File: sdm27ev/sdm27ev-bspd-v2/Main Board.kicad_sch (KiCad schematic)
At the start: 41 parts, among them IC301 L7805ACD2T-TR, IC302 74AHC1G08, IC303 SN74LVC1G17DBVRG4, IC304 SN74HC32PWR, U301 TLV9022QDRQ1

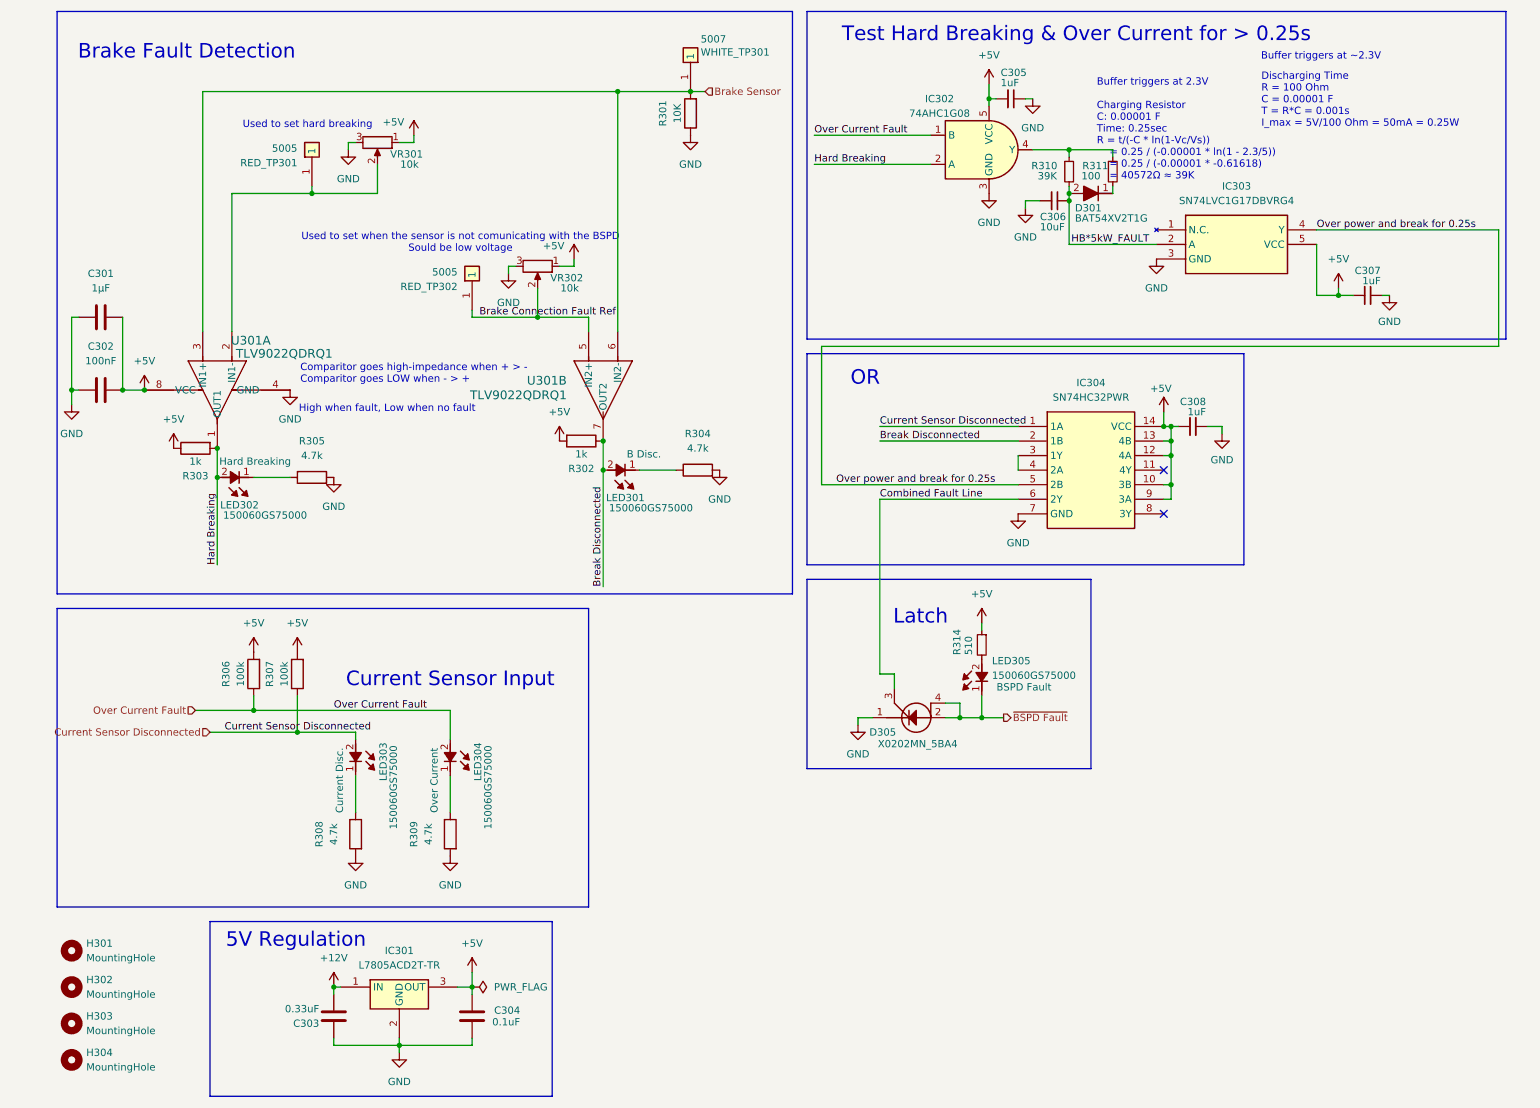
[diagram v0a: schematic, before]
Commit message: Reflow numbers and page order
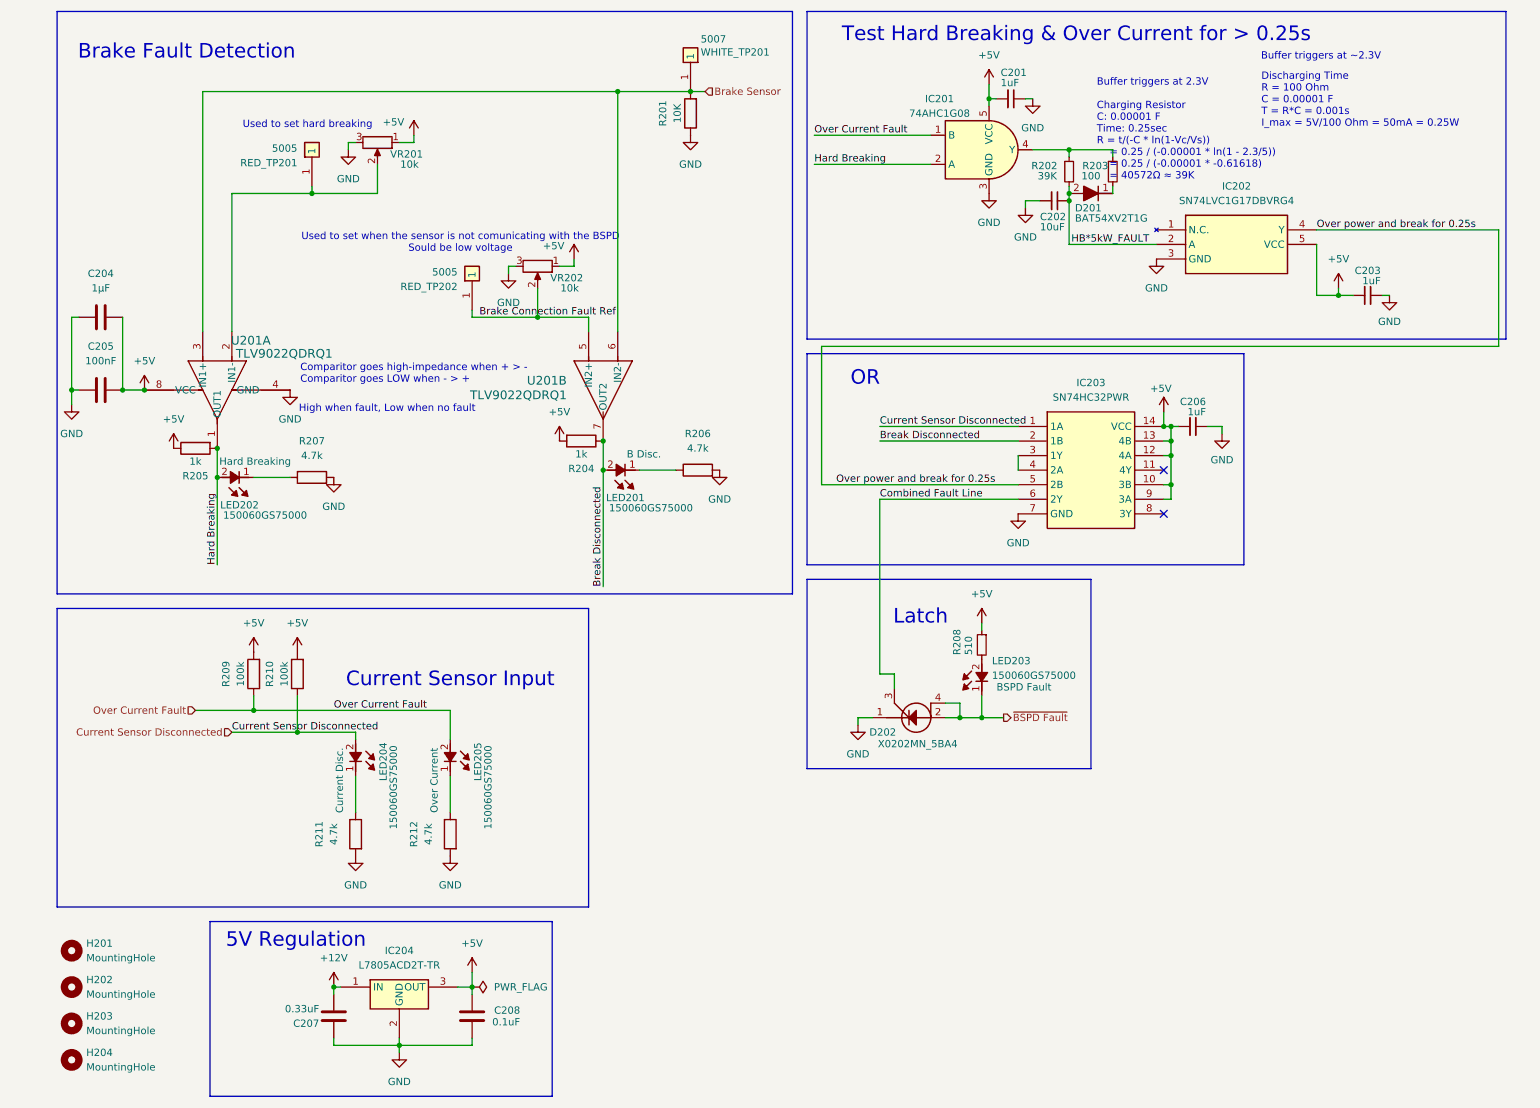
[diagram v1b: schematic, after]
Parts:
- renumbered C305 to C201, C306 to C202, C307 to C203, C301 to C204, C302 to C205, C308 to C206, C303 to C207, C304 to C208, D301 to D201, D305 to D202, H301 to H201, H302 to H202, H303 to H203, H304 to H204, IC302 to IC201, IC303 to IC202, IC304 to IC203, IC301 to IC204, LED301 to LED201, LED302 to LED202, LED305 to LED203, LED303 to LED204, LED304 to LED205, R301 to R201, R310 to R202, R311 to R203, R302 to R204, R303 to R205, R304 to R206, R305 to R207, R314 to R208, R306 to R209, R307 to R210, R308 to R211, R309 to R212, RED_TP301 to RED_TP201, RED_TP302 to RED_TP202, U301 to U201, VR301 to VR201, VR302 to VR202, WHITE_TP301 to WHITE_TP201

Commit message: small referance changes
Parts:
- C204, C205: footprint (none) -> Capacitor_SMD:C_0603_1608Metric
- H201, H202, H203, H204: footprint (none) -> MountingHole:MountingHole_2.2mm_M2_DIN965_Pad
- IC202: footprint SOT95P280X145-5N -> SDM_MiscFootprint:SOT95P280X145-5L
- R201, R204, R205, R206, R207, R209, R210, R211, R212: footprint (none) -> Resistor_SMD:R_0603_1608Metric
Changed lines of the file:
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@@
 	(text "Latch"
 		(exclude_from_sim no)
-		(at 164.592 119.634 0)
+		(at 165.608 119.634 0)
 		(effects
 			(font
@@
 	(wire
 		(pts
-			(xy 157.48 99.06) (xy 157.48 129.54)
-		)
-		(stroke
-			(width 0)
-			(type default)
-		)
-	)
-	(wire
-		(pts
 			(xy 62.23 184.15) (xy 63.5 184.15)
 		)
@@
 	(wire
 		(pts
-			(xy 160.02 129.54) (xy 160.02 132.08)
+			(xy 160.02 99.06) (xy 160.02 132.08)
 		)
 		(stroke
@@
 	(wire
 		(pts
-			(xy 160.02 129.54) (xy 157.48 129.54)
-		)
-		(stroke
-			(width 0)
-			(type default)
-		)
-	)
-	(wire
-		(pts
 			(xy 55.88 139.7) (xy 55.88 133.35)
 		)
@@
 	(wire
 		(pts
-			(xy 157.48 99.06) (xy 181.61 99.06)
+			(xy 160.02 99.06) (xy 181.61 99.06)
 		)
 		(stroke
@@
 	)
 	(label "Combined Fault Line"
-		(at 157.48 99.06 0)
+		(at 160.02 99.06 0)
 		(effects
 			(font
@@
 			)
 		)
-		(property "Footprint" ""
+		(property "Footprint" "MountingHole:MountingHole_2.2mm_M2_DIN965_Pad"
 			(at 16.51 196.85 0)
 			(hide yes)
@@
 			)
 		)
-		(property "Footprint" ""
+		(property "Footprint" "Resistor_SMD:R_0603_1608Metric"
 			(at 105.41 87.122 90)
 			(hide yes)
@@
 			)
 		)
-		(property "Footprint" ""
+		(property "Footprint" "Capacitor_SMD:C_0603_1608Metric"
 			(at 17.78 79.0448 0)
 			(hide yes)
@@
 			)
 		)
-		(property "Footprint" ""
+		(property "Footprint" "Resistor_SMD:R_0603_1608Metric"
 			(at 126.238 31.75 90)
 			(hide yes)
@@
 			)
 		)
-		(property "Footprint" ""
+		(property "Footprint" "Resistor_SMD:R_0603_1608Metric"
 			(at 67.818 157.48 90)
 			(hide yes)
@@
 			)
 		)
-		(property "Footprint" ""
+		(property "Footprint" "MountingHole:MountingHole_2.2mm_M2_DIN965_Pad"
 			(at 16.51 184.15 0)
 			(hide yes)
@@
 			)
 		)
-		(property "Footprint" ""
+		(property "Footprint" "Capacitor_SMD:C_0603_1608Metric"
 			(at 17.78 66.3448 0)
 			(hide yes)
@@
 			)
 		)
-		(property "Footprint" ""
+		(property "Footprint" "Resistor_SMD:R_0603_1608Metric"
 			(at 38.1 88.392 90)
 			(hide yes)
@@
 			)
 		)
-		(property "Footprint" ""
+		(property "Footprint" "Resistor_SMD:R_0603_1608Metric"
 			(at 84.328 157.48 90)
 			(hide yes)
@@
 			)
 		)
-		(property "Footprint" ""
+		(property "Footprint" "MountingHole:MountingHole_2.2mm_M2_DIN965_Pad"
 			(at 16.51 190.5 0)
 			(hide yes)
@@
 			)
 		)
-		(property "Footprint" ""
+		(property "Footprint" "Resistor_SMD:R_0603_1608Metric"
 			(at 50.038 129.54 90)
 			(hide yes)
@@
 			)
 		)
-		(property "Footprint" ""
+		(property "Footprint" "Resistor_SMD:R_0603_1608Metric"
 			(at 58.42 97.028 90)
 			(hide yes)
@@
 			)
 		)
-		(property "Footprint" ""
+		(property "Footprint" "MountingHole:MountingHole_2.2mm_M2_DIN965_Pad"
 			(at 16.51 177.8 0)
 			(hide yes)
@@
 			)
 		)
-		(property "Footprint" ""
+		(property "Footprint" "Resistor_SMD:R_0603_1608Metric"
 			(at 57.658 129.54 90)
 			(hide yes)
@@
 			)
 		)
-		(property "Footprint" ""
+		(property "Footprint" "Resistor_SMD:R_0603_1608Metric"
 			(at 125.73 95.758 90)
 			(hide yes)
@@
 			)
 		)
-		(property "Footprint" "SOT95P280X145-5N"
+		(property "Footprint" "SDM_MiscFootprint:SOT95P280X145-5L"
 			(at 229.87 146.99 0)
 			(hide yes)

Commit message: Fixed? latch logic voltage levels
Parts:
- added R213: 4.7k, Resistor_SMD:R_0603_1608Metric, symbol Device:R
- LED203: Measure BSPD Fault -> BSPD Good
- R208: value 510 -> 240
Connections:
- net GND: now also R213.2
- net ~{BSPD Fault}: now also LED203.2 (A), R208.2; no longer LED203.1 (K)
- new net: LED203.1 (K), R213.1
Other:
- note added: "5V / 20mA = 250Ω"
- moved on the sheet: D202, R208

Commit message: current limiting resistor
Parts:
- added R208: 4.7k, symbol Device:R
- renumbered R208 to R209, R209 to R210, R210 to R211, R213 to R212, R211 to R213, R212 to R214
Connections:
- net Combined Fault Line: now also R208.1; no longer D202.3 (G)
- new net: D202.3 (G), R208.2
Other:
- note added: "Gate current: 200µA < I < 20mA Voltage loss: <0.8V 4.2V/4.7kΩ = 0.9mA"
- moved on the sheet: D202, LED203, R209, R212

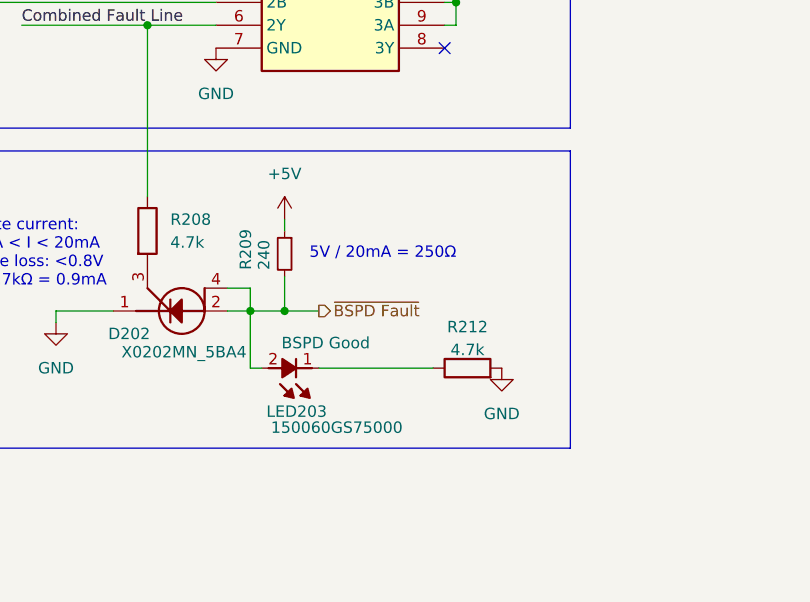
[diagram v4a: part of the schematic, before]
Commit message: BSPD SCR latch
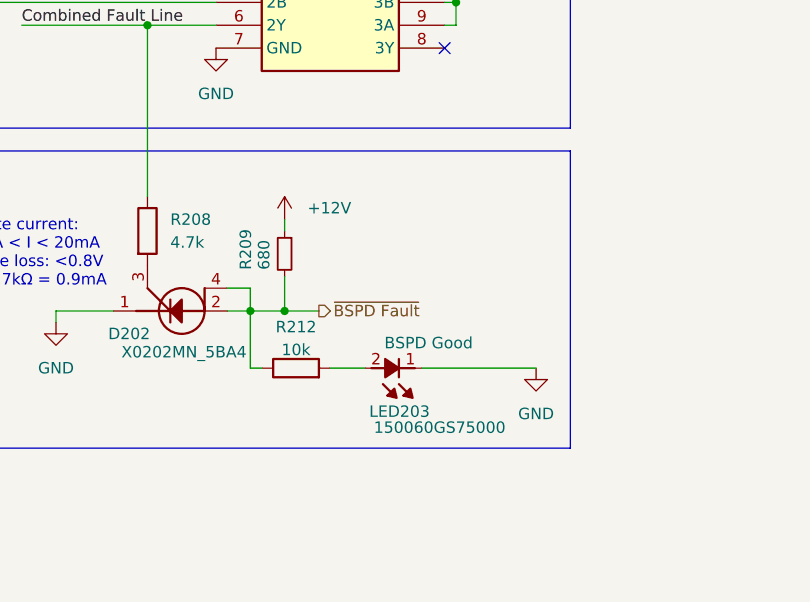
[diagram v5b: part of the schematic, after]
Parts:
- R209: value 240 -> 680
- R212: value 4.7k -> 10k
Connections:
- net +12V: now also R209.1
- net +5V: no longer R209.1
- net GND: now also LED203.1 (K); no longer R212.2
- net ~{BSPD Fault}: now also R212.1; no longer LED203.2 (A)
- new net: LED203.2 (A), R212.2
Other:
- note removed: "5V / 20mA = 250Ω"
